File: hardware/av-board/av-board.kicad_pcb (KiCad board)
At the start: 2 copper layers, 99.1 x 99.1 mm, 15 parts, among them P1 D0..D7, P2 A0..A7, P3 CTRL1, P4 A8..A15, P5 A16..A23, P6 CTRL2, U1 74HC138, U2 WD65C22, U3 74HC00, U4 74HC138

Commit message: add work on VDP board
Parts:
- added C1: 27pF, Capacitors_SMD:C_0603_HandSoldering, F.Cu at (161.9, 73.7)
- added C2: 27pF, Capacitors_SMD:C_0603_HandSoldering, F.Cu at (161.9, 68.6)
- added D2: D_Small, Diodes_SMD:SMA-SMB_Universal_Handsoldering, F.Cu at (238.8, 76.8)
- added U10: CY62256, Housings_SOIC:SOIC-28W_7.5x17.9mm_Pitch1.27mm, F.Cu at (173.4, 106.0)
- added U5: 74HC04, Housings_SOIC:SOIC-14_3.9x8.7mm_Pitch1.27mm, F.Cu at (160.7, 114.9)
- added U6: TMS9929, Housings_DIP:DIP-40_W15.24mm_LongPads, F.Cu at (136.5, 68.6)
- added U7: 74LS574, Housings_SOIC:SOIC-20W_7.5x12.8mm_Pitch1.27mm, F.Cu at (160.7, 88.3)
- added U8: 74LS574, Housings_SOIC:SOIC-20W_7.5x12.8mm_Pitch1.27mm, F.Cu at (160.7, 103.5)
- added U9: 74LS574, Housings_SOIC:SOIC-20W_7.5x12.8mm_Pitch1.27mm, F.Cu at (173.4, 88.3)
- added Y1: 10.7MHz, Crystals:Crystal_HC49-U_Vertical, F.Cu at (156.8, 71.0)
- moved U3 83.2 mm to (94.0, 62.9)
- moved U2 27.8 mm to (104.1, 67.3)
- moved D1 20.1 mm to (96.5, 109.2)
- moved U4 15.3 mm to (95.9, 78.1)
- moved U1 5.28 mm to (92.1, 92.7)
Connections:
- U3 pad 4: (no net) -> /Video/SEL
- U3 pad 6: (no net) -> /Video/~CSR
- U3 pad 8: (no net) -> /Video/~CSW
- U3 pad 9: (no net) -> /Video/SEL
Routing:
- net Net-(U6-Pad4): track 0.00 -> 123.6 mm, vias 0 -> 10
- net /Video/R/~W: track 0.00 -> 114.4 mm, vias 0 -> 10
- net Net-(U6-Pad5): track 0.00 -> 101.8 mm, vias 0 -> 9
- net Net-(U6-Pad3): track 0.00 -> 97.5 mm, vias 0 -> 7
- net /Video/~CAS: track 0.00 -> 89.2 mm, vias 0 -> 4
- net Net-(U6-Pad6): track 0.00 -> 86.4 mm, vias 0 -> 9
- net Net-(U6-Pad9): track 0.00 -> 78.6 mm, vias 0 -> 7
- net +5V: track 0.00 -> 77.4 mm, vias 0 -> 4
- net /Video/~RAS: track 0.00 -> 76.7 mm, vias 0 -> 4
- net Net-(U6-Pad8): track 0.00 -> 70.0 mm, vias 0 -> 6
- net /Video/VD0: track 0.00 -> 67.4 mm, vias 0 -> 5
- net Net-(U6-Pad7): track 0.00 -> 67.3 mm, vias 0 -> 7
- net /Video/VD1: track 0.00 -> 64.6 mm, vias 0 -> 5
- net /Video/VD2: track 0.00 -> 60.5 mm, vias 0 -> 3
- net Net-(U6-Pad10): track 0.00 -> 60.1 mm, vias 0 -> 4
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
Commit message: start to wire up VDP
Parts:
- added P7: R, w_conn_av:rca_black, F.Cu at (144.1, 55.9)
- added P8: G, w_conn_av:rca_black, F.Cu at (169.5, 55.9)
- added P9: B, w_conn_av:rca_black, F.Cu at (156.8, 55.9)
- added R1: 330, Resistors_SMD:R_0603_HandSoldering, F.Cu at (161.5, 155.6)
- added R2: 330, Resistors_SMD:R_0603_HandSoldering, F.Cu at (196.2, 154.3)
- added R3: 330, Resistors_SMD:R_0603_HandSoldering, F.Cu at (135.3, 157.4)
- added U3: 74HC00, Housings_SOIC:SOIC-14_3.9x8.7mm_Pitch1.27mm, F.Cu at (158.1, 73.7)
- moved D2 122.2 mm to (127.6, 127.6)
- moved C1 11.7 mm to (150.5, 76.2), turned to 90 degrees
- moved C2 11.7 mm to (150.5, 71.1), turned to 270 degrees
- moved U6 10.5 mm to (126.4, 71.1)
- moved U7 10.5 mm to (150.5, 90.8)
- moved U8 10.5 mm to (150.5, 106.0)
- moved U9 10.5 mm to (163.2, 90.8)
- moved Y1 10.5 mm to (146.7, 73.6)
- moved U10 10.5 mm to (163.2, 108.6)
- moved U5 10.5 mm to (150.5, 117.5)
- renumbered U3 to U11
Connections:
- net /Video/R/~W renamed /Video/VR/~W
- U11 pad 4: /Video/SEL -> (no net)
- U11 pad 6: /Video/~CSR -> (no net)
- U11 pad 8: /Video/~CSW -> (no net)
- U11 pad 9: /Video/SEL -> (no net)
- U4 pad 15: (no net) -> /~VDPS
- U6 pad 17: /D7 -> (no net)
- U6 pad 18: /D6 -> (no net)
- U6 pad 19: /D5 -> (no net)
- U6 pad 20: /D4 -> (no net)
- U6 pad 21: /D3 -> (no net)
- U6 pad 22: /D2 -> (no net)
- U6 pad 23: /D1 -> (no net)
- U6 pad 24: /D0 -> (no net)
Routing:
- net /Video/~CSW: track 0.00 -> 67.3 mm, vias 0 -> 4
- net /Video/~CSR: track 0.00 -> 66.2 mm, vias 0 -> 3
- net /Video/VR/~W: track 114.4 -> 90.8 mm, vias 10 -> 5
- net +5V: track 77.4 -> 93.3 mm, vias 4 -> 5
- net Net-(U3-Pad1): track 0.00 -> 13.1 mm, vias 0 -> 2
- net Net-(U3-Pad2): track 0.00 -> 11.4 mm, vias 0 -> 2
- net Net-(U6-Pad3): track 97.5 -> 89.3 mm, vias 7 -> 5
- net /R/~W: track 0.00 -> 6.50 mm
- net Net-(C1-Pad2): track 11.7 -> 10.2 mm
- net Net-(C2-Pad2): track 10.7 -> 9.28 mm
- net GND: track 15.3 -> 15.4 mm, vias 9 -> 11
- net Net-(U6-Pad5): vias 9 -> 8

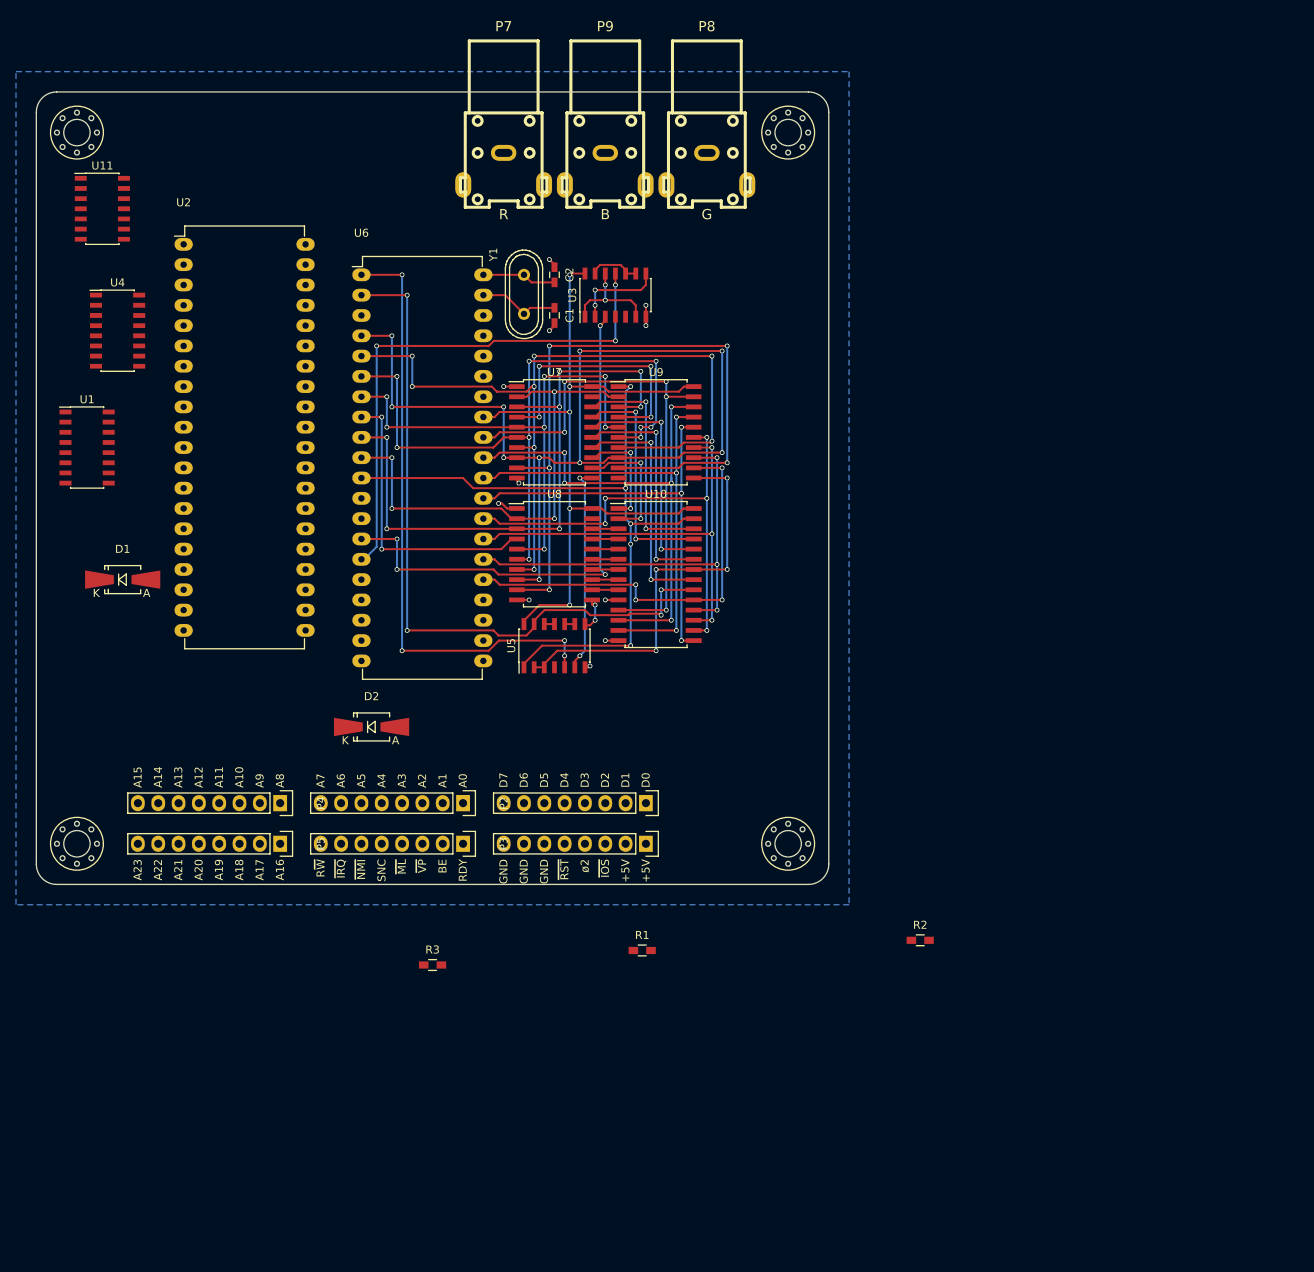
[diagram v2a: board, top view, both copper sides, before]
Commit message: add first pass at sound wiring
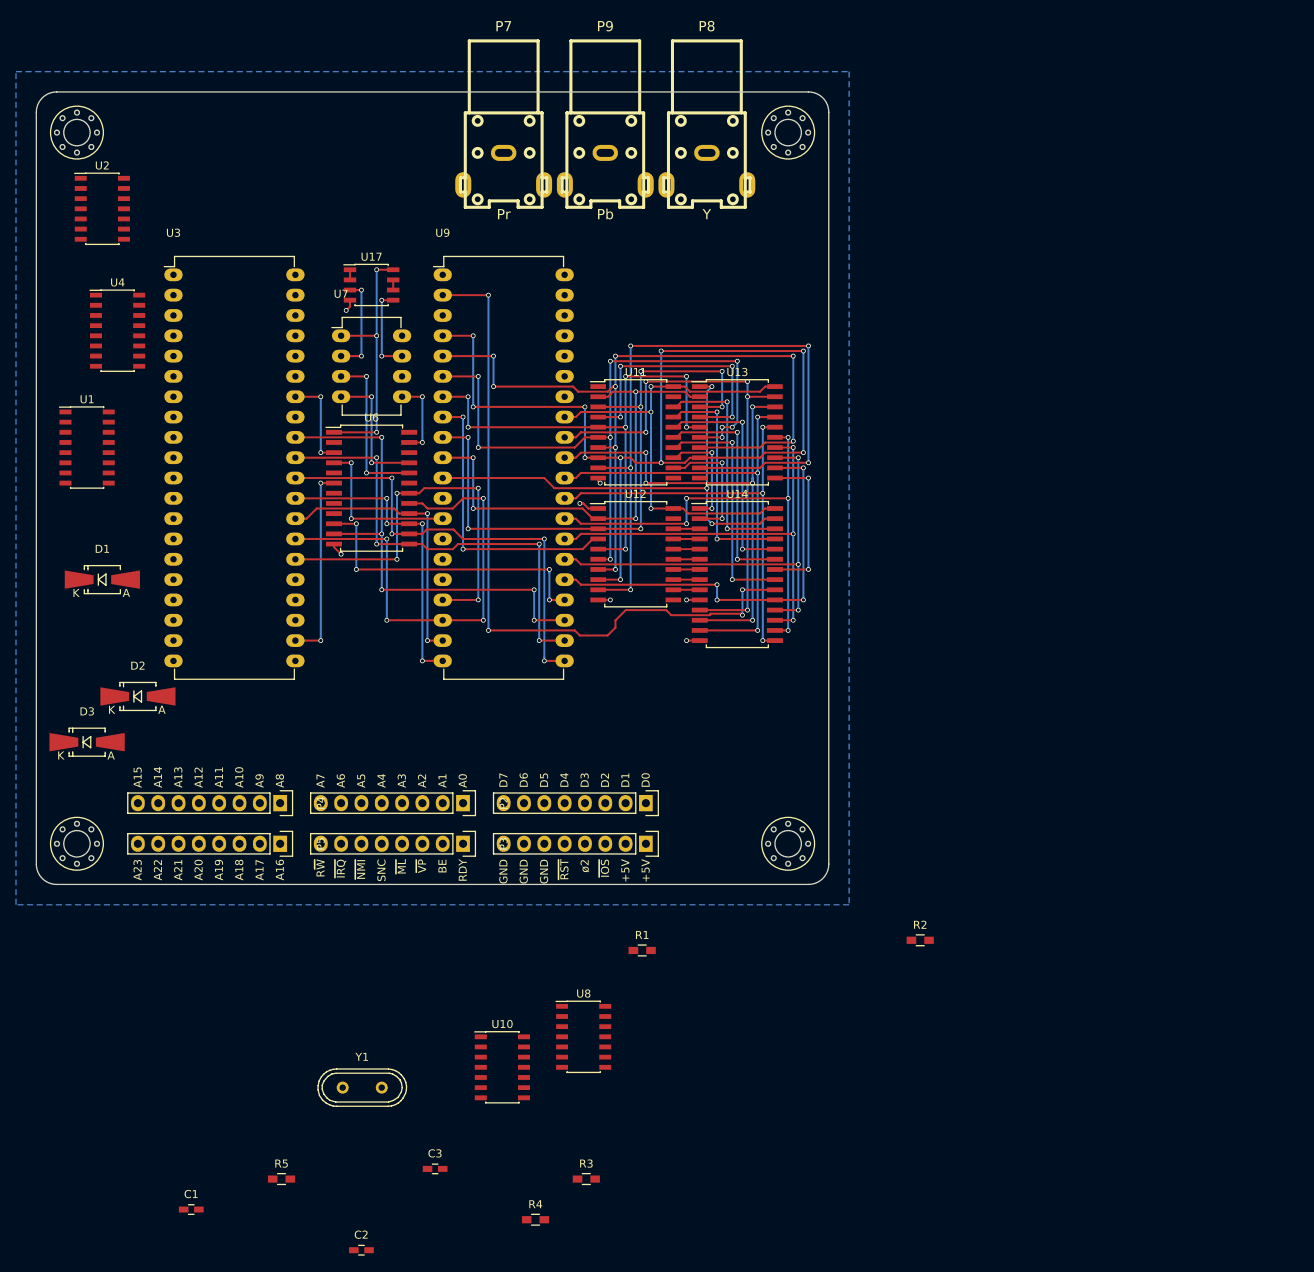
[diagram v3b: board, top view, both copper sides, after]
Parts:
- removed the U3 at (158.1, 73.7)
- removed U5: 74HC04, Housings_SOIC:SOIC-14_3.9x8.7mm_Pitch1.27mm
- added C3: 100n, Capacitors_SMD:C_0603_HandSoldering, F.Cu at (135.6, 182.9)
- added D2: D_Small, Diodes_SMD:SMA-SMB_Universal_Handsoldering, F.Cu at (98.4, 123.8)
- added R4: 1K, Resistors_SMD:R_0603_HandSoldering, F.Cu at (148.1, 189.2)
- added R5: 1K, Resistors_SMD:R_0603_HandSoldering, F.Cu at (116.4, 184.2)
- added U10: 74HC00, Housings_SOIC:SOIC-14_3.9x8.7mm_Pitch1.27mm, F.Cu at (144.0, 170.2)
- added U17: TL072, Housings_SOIC:SOIC-8_3.9x4.9mm_Pitch1.27mm, F.Cu at (127.6, 72.4)
- added U6: YM3812, Housings_SOIC:SOIC-24W_7.5x15.4mm_Pitch1.27mm, F.Cu at (127.6, 97.8)
- added U7: YM3014, Housings_DIP:DIP-8_W7.62mm_LongPads, F.Cu at (123.8, 78.7)
- added U8: 74HC04, Housings_SOIC:SOIC-14_3.9x8.7mm_Pitch1.27mm, F.Cu at (154.1, 166.4)
- P7: value R -> Pr
- P8: value G -> Y
- P9: value B -> Pb
- Y1: value 10.7MHz -> 21.48MHz
- moved C2 124.3 mm to (126.4, 193.0), turned to 0 degrees
- moved C1 120.6 mm to (105.1, 188.0), turned to 0 degrees
- moved Y1 101.2 mm to (126.5, 172.7), turned to 0 degrees
- moved D3 35.6 mm to (92.1, 129.5)
- moved R3 32.9 mm to (154.5, 184.2)
- moved U9 10.2 mm to (136.5, 71.1)
- moved U11 10.2 mm to (160.7, 90.8)
- moved U12 10.2 mm to (160.7, 106.0)
- moved U13 10.2 mm to (173.4, 90.8)
- moved U14 10.2 mm to (173.4, 108.6)
- moved U3 4.02 mm to (102.9, 71.1)
- moved D1 2.54 mm to (94.0, 109.2)
- renumbered D2 to D3, U7 to U11, U8 to U12, U9 to U13, U10 to U14, U11 to U2, U2 to U3, U6 to U9
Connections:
- U11 pad 11: /Video/ROW -> (no net)
- U4 pad 14: (no net) -> /~SNDS
- U4 pad 15: /~VDPS -> (no net)
- U9 pad 1: /Video/~RAS -> (no net)
- U9 pad 17: (no net) -> /D7
- U9 pad 18: (no net) -> /D6
- U9 pad 19: (no net) -> /D5
- U9 pad 20: (no net) -> /D4
- U9 pad 21: (no net) -> /D3
- U9 pad 22: (no net) -> /D2
- U9 pad 23: (no net) -> /D1
- U9 pad 24: (no net) -> /D0
- U9 pad 39: Net-(C1-Pad2) -> (no net)
- U9 pad 40: Net-(C2-Pad2) -> (no net)
- Y1 pad 1: Net-(C1-Pad2) -> Net-(C2-Pad2)
- Y1 pad 2: Net-(C2-Pad2) -> Net-(C1-Pad2)
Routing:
- net /Video/~RAS: track 76.7 -> 0.00 mm, vias 4 -> 0
- net /Video/~CSW: track 67.3 -> 0.00 mm, vias 4 -> 0
- net /Video/~CSR: track 66.2 -> 0.35 mm, vias 3 -> 0
- net /D1: track 0.00 -> 62.5 mm, vias 0 -> 5
- net /D6: track 0.00 -> 59.0 mm, vias 0 -> 4
- net /D2: track 0.00 -> 57.0 mm, vias 0 -> 4
- net /D3: track 0.00 -> 56.6 mm, vias 0 -> 4
- net /D7: track 0.00 -> 49.8 mm, vias 0 -> 4
- net /D4: track 0.00 -> 38.7 mm, vias 0 -> 4
- net /D0: track 0.00 -> 38.4 mm, vias 0 -> 4
- net /D5: track 0.00 -> 35.1 mm, vias 0 -> 2
- net /Video/WR: track 51.0 -> 19.8 mm, vias 4 -> 2
- net /Video/VR/~W: track 90.8 -> 60.9 mm, vias 5 -> 3
- net /Video/ROW: track 26.0 -> 0.00 mm, vias 2 -> 0
- net Net-(U6-Pad20): track 0.00 -> 20.6 mm, vias 0 -> 2
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
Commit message: add SPI keyboard output
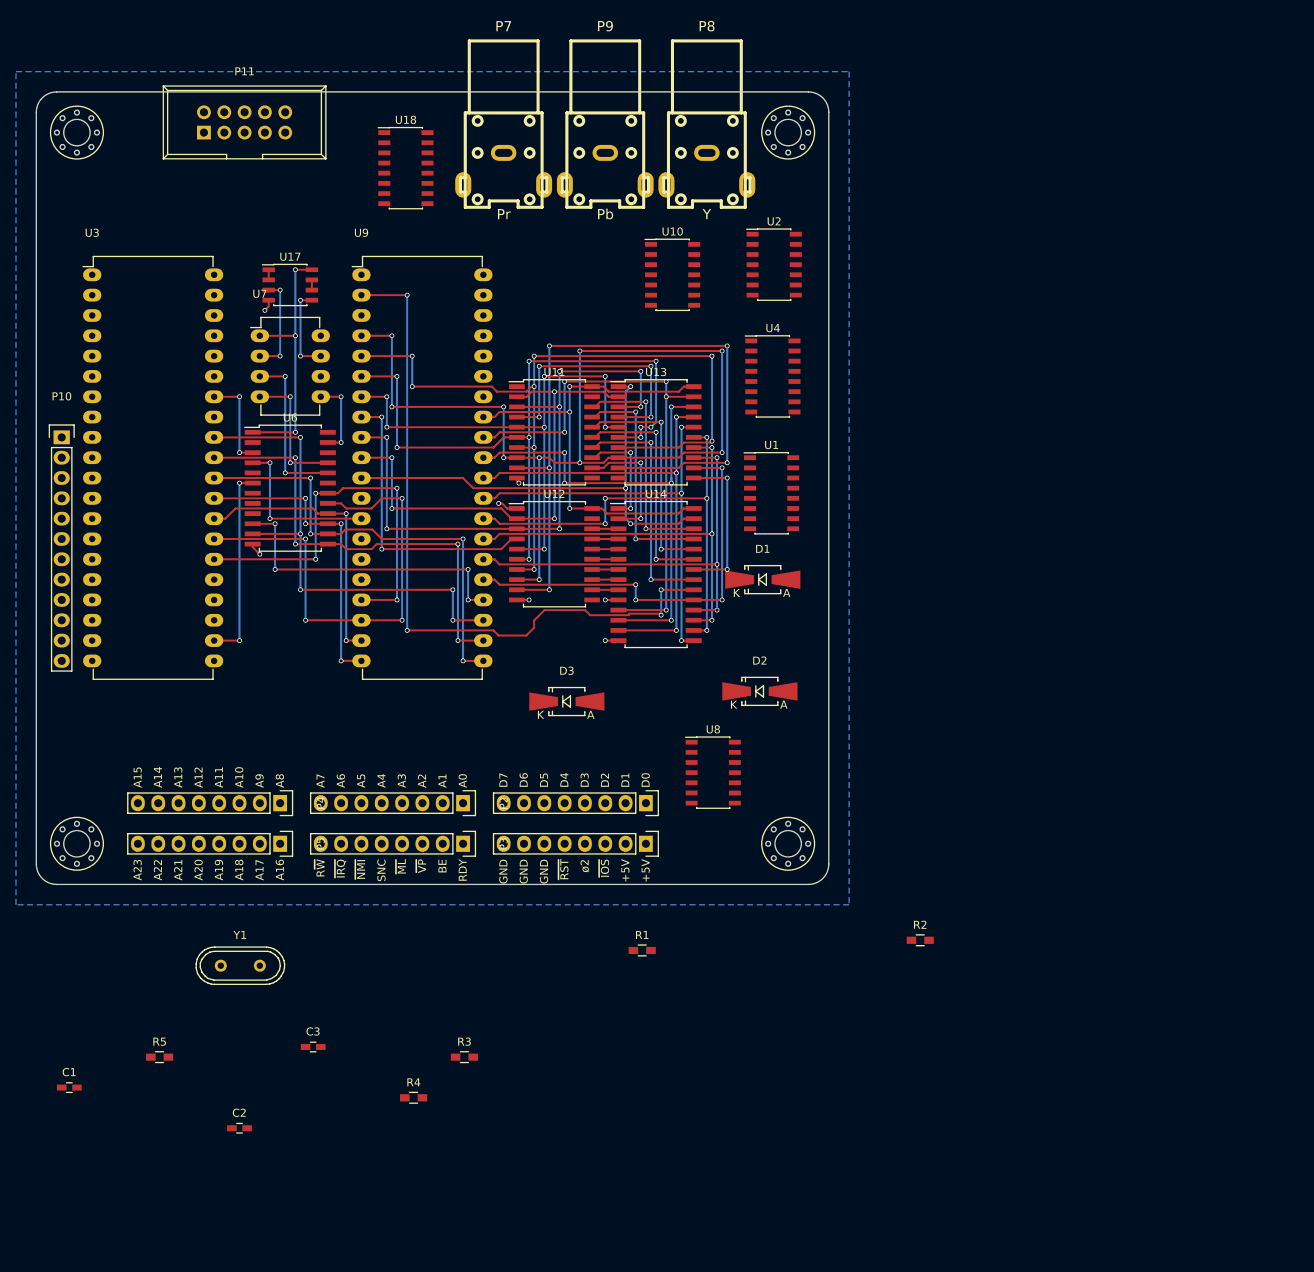
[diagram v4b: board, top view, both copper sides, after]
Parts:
- added P10: PARALLEL, Pin_Headers:Pin_Header_Straight_1x12, F.Cu at (88.9, 91.4)
- added P11: KEYBOARD, Connect:IDC_Header_Straight_10pins, F.Cu at (106.7, 53.3)
- added U18: 74HC138, Housings_SOIC:SOIC-16_3.9x9.9mm_Pitch1.27mm, F.Cu at (131.9, 57.8)
- moved U10 101.3 mm to (165.3, 71.1)
- moved U1 85.8 mm to (177.6, 98.4)
- moved U2 84.3 mm to (178.0, 69.8)
- moved D1 82.5 mm to (176.5, 109.2)
- moved U4 82.1 mm to (177.8, 83.8)
- moved D2 77.7 mm to (176.2, 123.2)
- moved D3 60.2 mm to (152.0, 124.5)
- moved U8 36.8 mm to (170.3, 133.3)
- moved Y1 21.6 mm to (111.2, 157.5)
- moved C1 21.6 mm to (89.9, 172.7)
- moved C3 21.6 mm to (120.3, 167.6)
- moved R5 21.6 mm to (101.1, 168.9)
- moved R3 21.6 mm to (139.2, 168.9)
- moved R4 21.6 mm to (132.9, 174.0)
- moved C2 21.6 mm to (111.1, 177.8)
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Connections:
- U3 pad 10: (no net) -> Net-(P10-Pad2)
- U3 pad 11: (no net) -> Net-(P10-Pad3)
- U3 pad 12: (no net) -> Net-(P10-Pad4)
- U3 pad 13: (no net) -> Net-(P10-Pad5)
- U3 pad 14: (no net) -> Net-(P10-Pad6)
- U3 pad 15: (no net) -> Net-(P10-Pad7)
- U3 pad 16: (no net) -> Net-(P10-Pad8)
- U3 pad 17: (no net) -> Net-(P10-Pad9)
- U3 pad 18: (no net) -> Net-(P10-Pad10)
- U3 pad 19: (no net) -> Net-(P10-Pad11)
- U3 pad 2: (no net) -> /SPICLK
- U3 pad 3: (no net) -> /SPIMOSI
- U3 pad 39: (no net) -> /~SPIIRQ2
- U3 pad 4: (no net) -> Net-(U18-Pad1)
- U3 pad 5: (no net) -> Net-(U18-Pad2)
- U3 pad 6: (no net) -> Net-(U18-Pad3)
- U3 pad 9: (no net) -> /SPIMISO
